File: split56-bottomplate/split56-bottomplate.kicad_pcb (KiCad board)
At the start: 2 copper layers, 139.2 x 82 mm, 17 parts, among them J1 AudioJack4, J2 AudioJack4, J3 AudioJack4, J4 AudioJack4, SW1 SW_DIP_x02

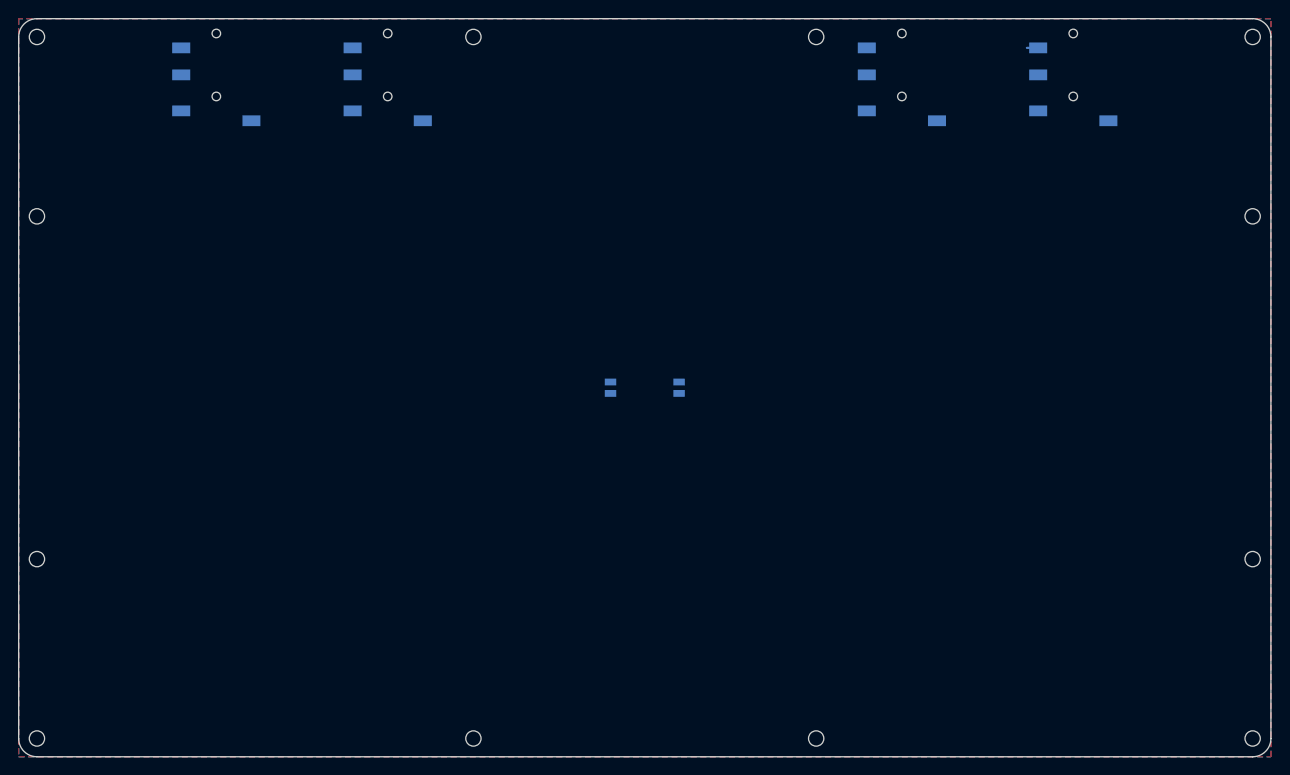
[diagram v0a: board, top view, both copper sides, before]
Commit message: Add Bottom Plate
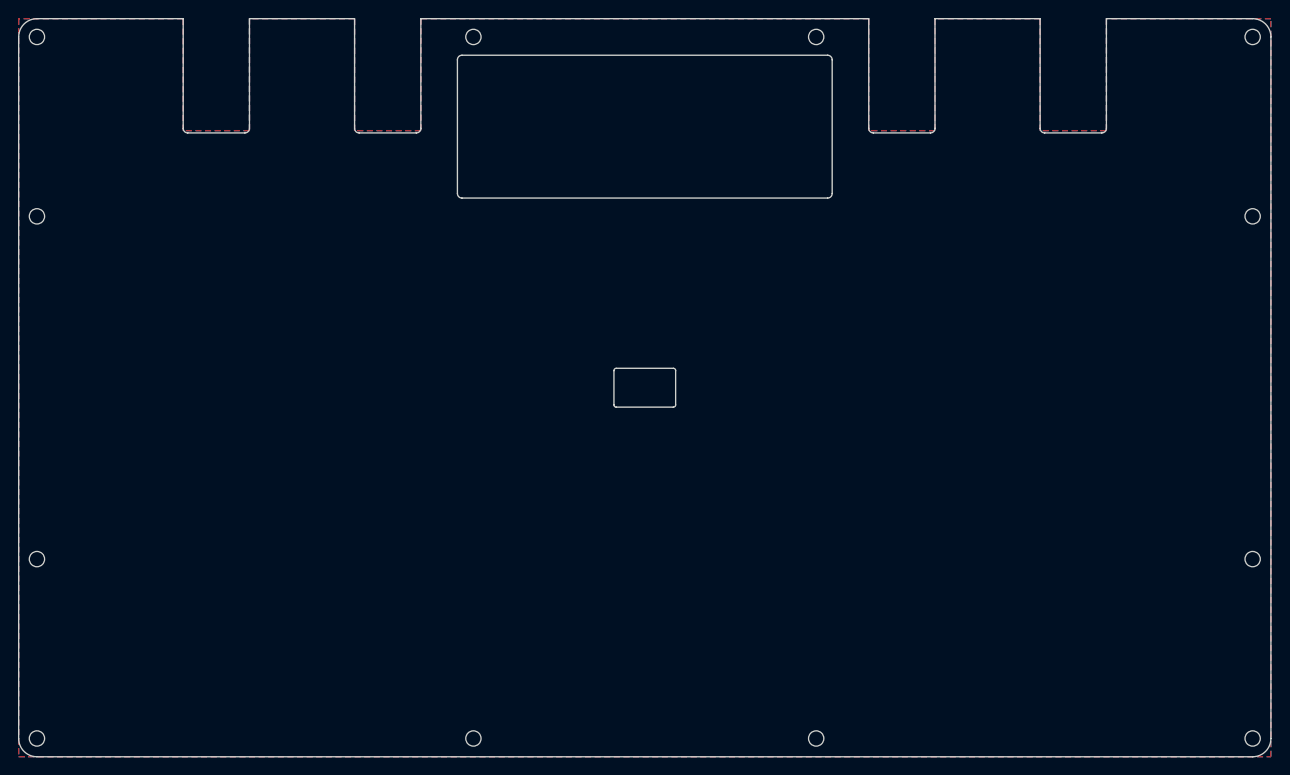
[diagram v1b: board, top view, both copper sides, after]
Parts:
- removed J1, J2, J3, J4: AudioJack4, library:TRRS_SMD_PJ320
- removed SW1: SW_DIP_x02, library:DipSwitch
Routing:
- net SDA: track 1.65 -> 0.00 mm
- added copper zone on B.Cu, net (none)
- added copper zone on F.Cu, net (none)
- removed copper zone on B.Cu, net GND
- removed copper zone on F.Cu, net GND
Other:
- outline, holes or cut-outs redrawn
